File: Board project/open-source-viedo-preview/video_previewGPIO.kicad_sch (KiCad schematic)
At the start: 21 parts, among them J10 7499110124, J11 Conn_02x20_Odd_Even, J12 Micro_SD_Card_Det, J7 Conn_02x07_Odd_Even, J8 Conn_01x03, J9 Conn_01x03, U1 74LVC1G07, U2 74LVC1G07

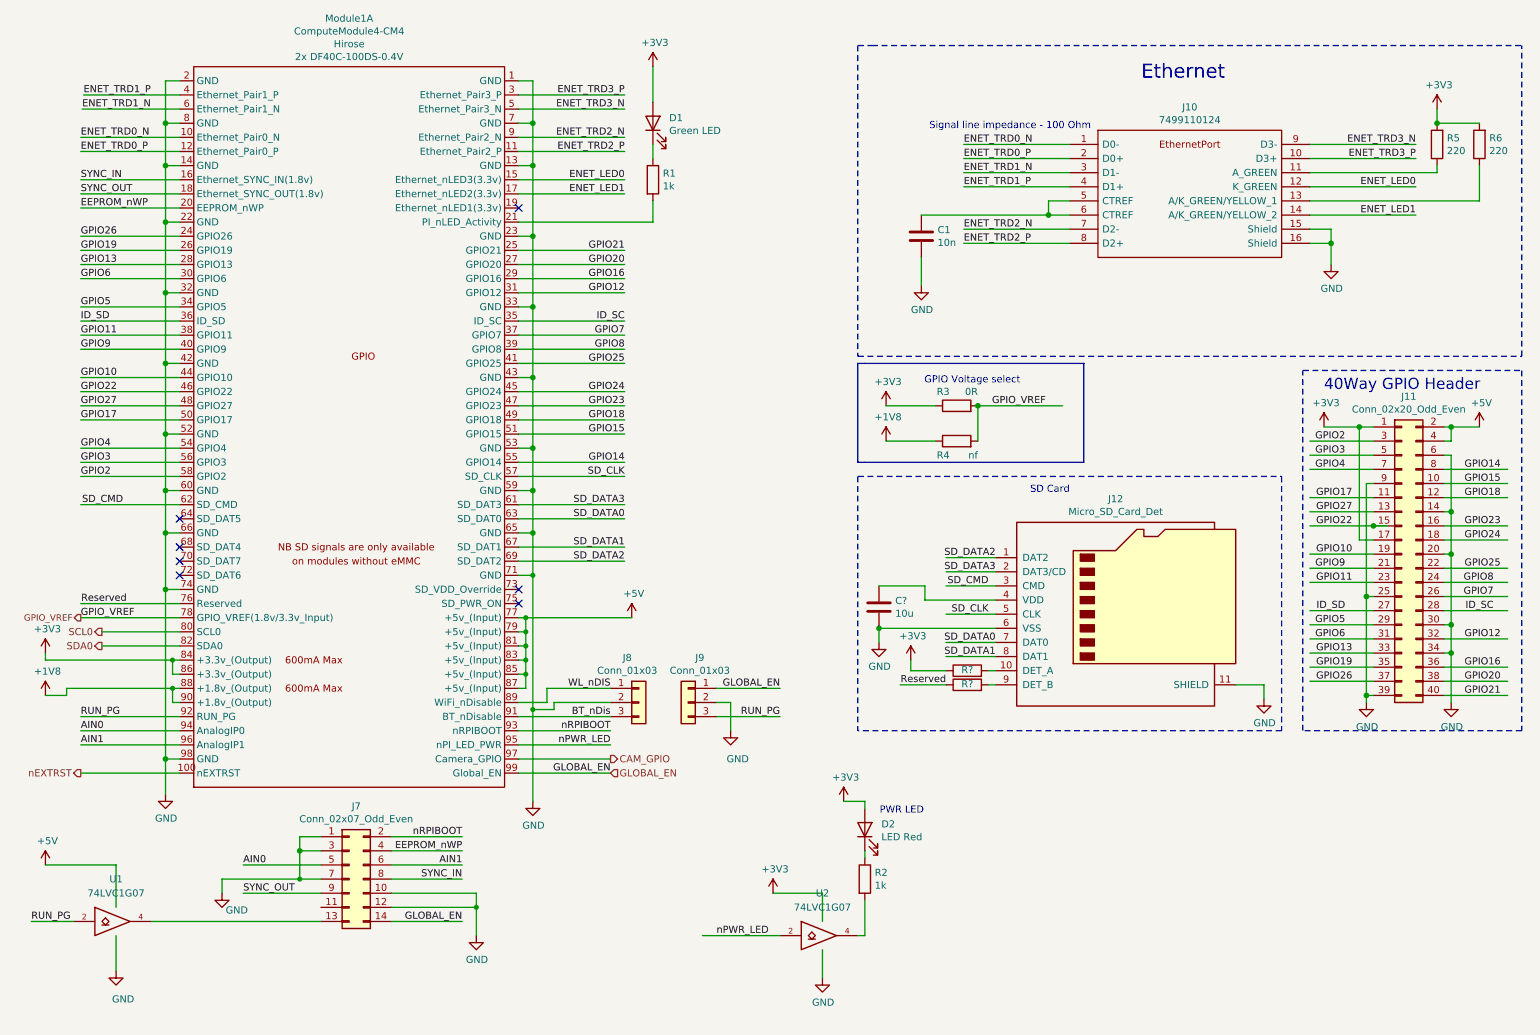
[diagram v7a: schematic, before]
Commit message: ERC error repaired
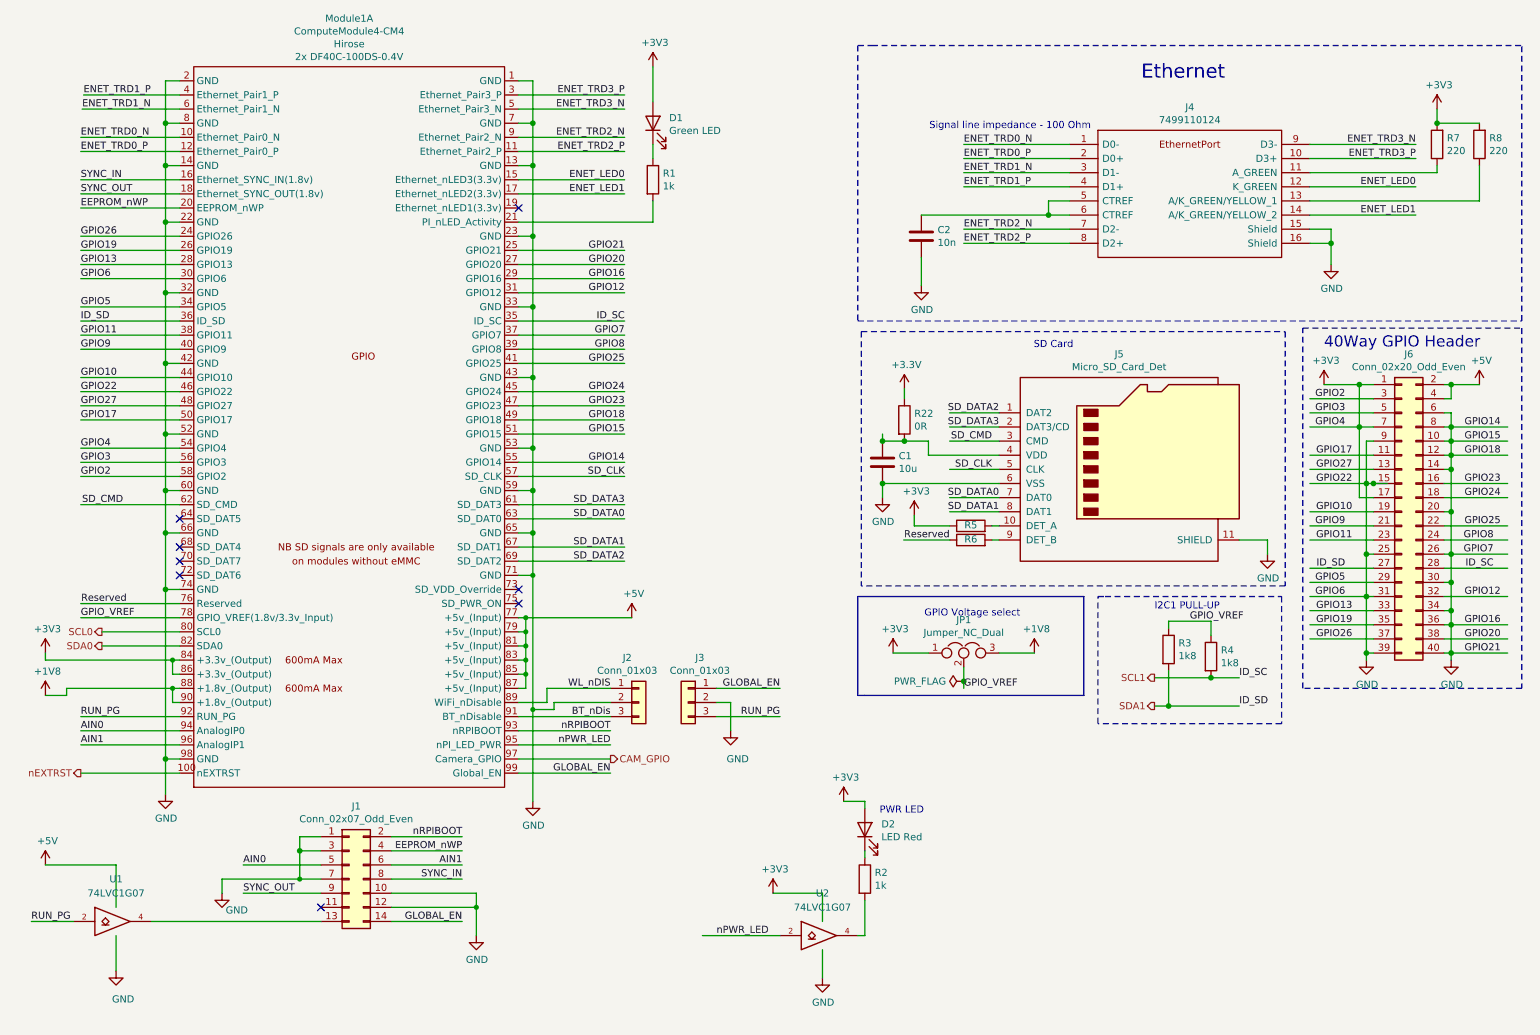
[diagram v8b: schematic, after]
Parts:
- added JP1: Jumper_NC_Dual, symbol Device:Jumper_NC_Dual
- added R22: 0R, symbol Device:R
- R3: value 0R -> 1k8; footprint Resistor_SMD:R_1206_3216Metric_Pad1.30x1.75mm_HandSolder -> (none); Field4 Farnell -> (none); Field5 9233750 -> (none); Field6 MCR10EZPJ000 -> (none); Field7 Rohm -> (none); Field8 121629591 -> (none); Part Description Resistor 0R M2012 5% -> (none)
- R4: value nf -> 1k8; footprint Resistor_SMD:R_0805_2012Metric_Pad1.15x1.40mm_HandSolder -> (none); Field4 nf -> (none); Field5 nf -> (none); Field6 nf -> (none)
- gave numbers to parts that had none: 3
- renumbered C1 to C2, J7 to J1, J8 to J2, J9 to J3, J10 to J4, J12 to J5, J11 to J6, R5 to R7, R6 to R8
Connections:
- net GPIO14 is gone; now on net GND: J6.8 (Pin_8), Module1.55 (GPIO14)
- net GPIO15 is gone; now on net GND: J6.10 (Pin_10), Module1.51 (GPIO15)
- net GPIO16 is gone; now on net GND: J6.36 (Pin_36), Module1.29 (GPIO16)
- net GPIO18 is gone; now on net GND: J6.12 (Pin_12), Module1.49 (GPIO18)
- net GPIO21 is gone; now on net GND: J6.40 (Pin_40), Module1.25 (GPIO21)
- net GPIO22 is gone; now on net GND: J6.15 (Pin_15), Module1.46 (GPIO22)
- net GPIO4 is gone; now on net +3V3: J6.7 (Pin_7), Module1.54 (GPIO4)
- net GPIO6 is gone; now on net GND: J6.31 (Pin_31), Module1.30 (GPIO6)
- net GPIO7 is gone; now on net GND: J6.26 (Pin_26), Module1.37 (GPIO7)
- net +1V8: now also JP1.3; no longer R4.1
- net +3V3: now also JP1.1, R22.1; no longer R3.1
- net GPIO_VREF: now also R3.1, R4.1, JP1.2; no longer R3.2, R4.2
- net at C1.1, J5.4 (VDD): now also R22.2
- net ID_SC renamed SCL1
- net SCL1: now also R4.2
- net ID_SD renamed SDA1
- net SDA1: now also R3.2
- no-connect marks 7 -> 8
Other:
- note added: "I2C1 PULL-UP"
- moved on the sheet: C1, J5, J6, R5, R6
